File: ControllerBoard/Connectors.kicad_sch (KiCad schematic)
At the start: 2 parts, among them J1 X0511WVS-24AS-LPV01, J2 X0511WVS-24AS-LPV01

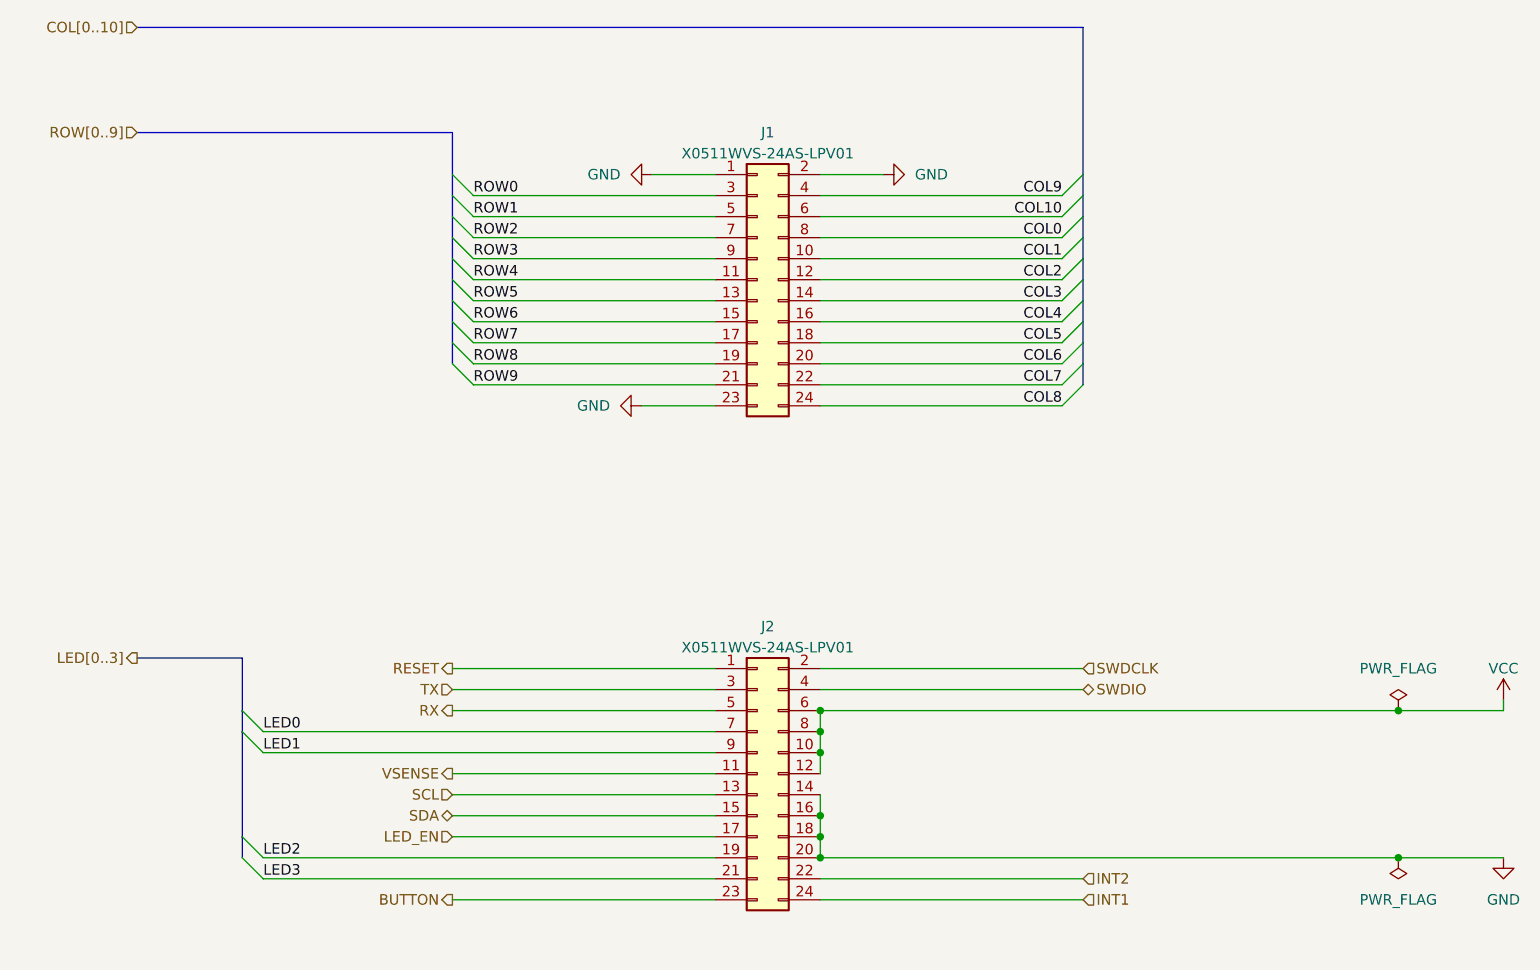
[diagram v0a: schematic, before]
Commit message: Remove LED driver
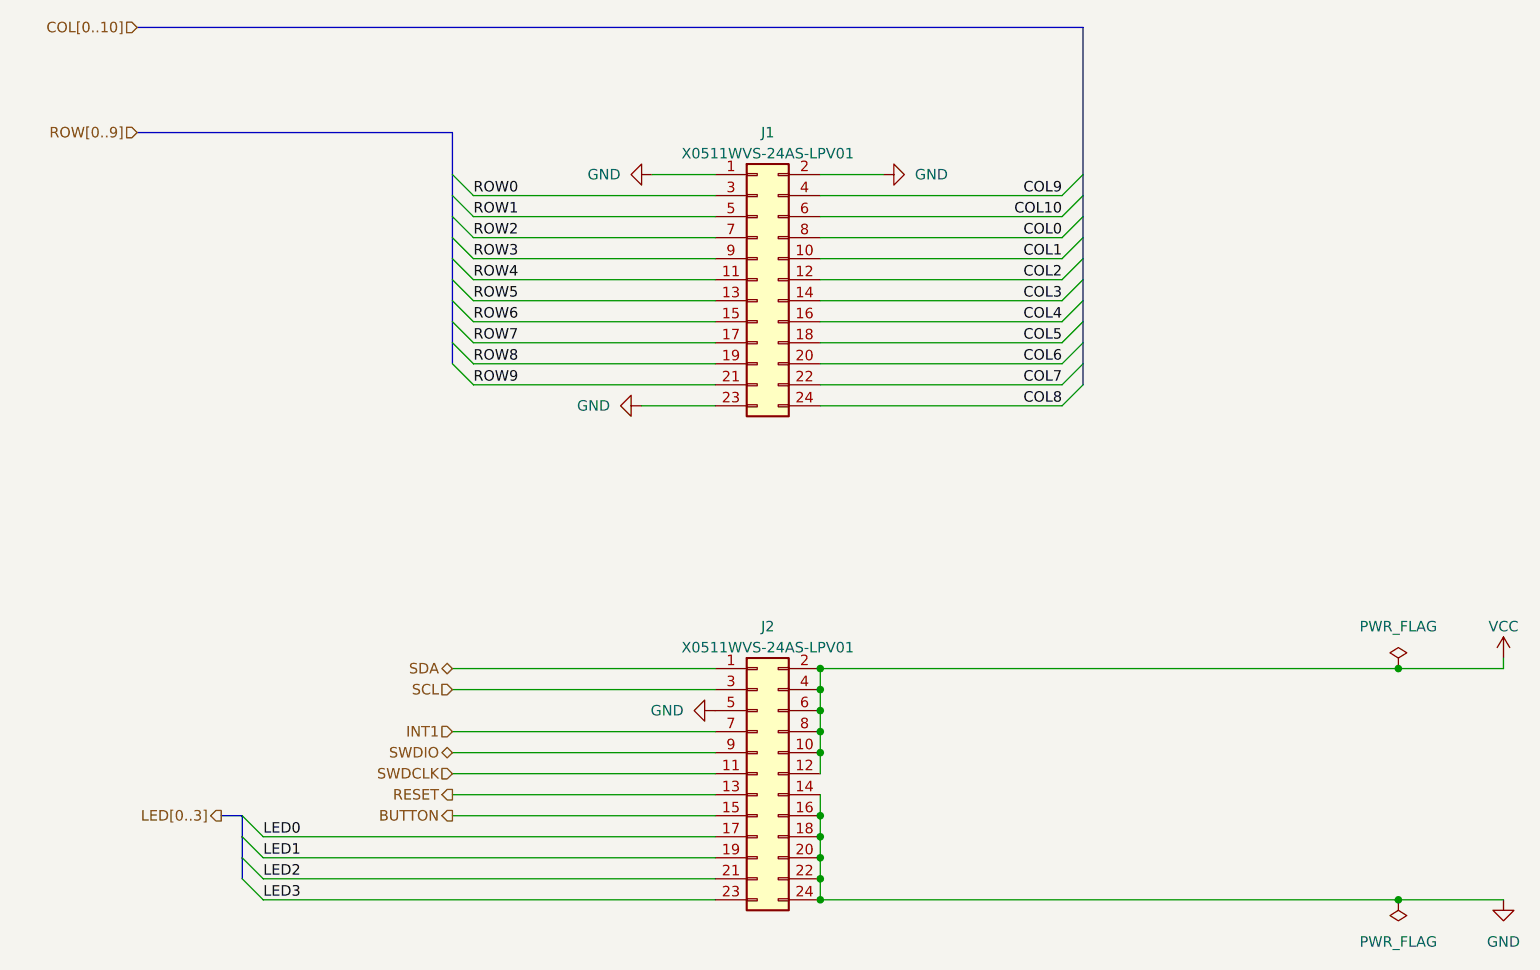
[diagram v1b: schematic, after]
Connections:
- net INT2 is gone; now on net GND: J2.22 (Pin_22)
- net LED_EN is gone; now on net LED0: J2.17 (Pin_17)
- net RX is gone; now on net GND: J2.5 (Pin_5)
- net TX is gone; now on net SCL: J2.3 (Pin_3)
- net VSENSE is gone; now on net SWDCLK: J2.11 (Pin_11)
- net BUTTON: now also J2.15 (Pin_15); no longer J2.23 (Pin_23)
- net GND: now also J2.24 (Pin_24)
- net INT1: now also J2.7 (Pin_7); no longer J2.24 (Pin_24)
- net LED0: no longer J2.7 (Pin_7)
- net LED1: now also J2.19 (Pin_19); no longer J2.9 (Pin_9)
- net LED2: now also J2.21 (Pin_21); no longer J2.19 (Pin_19)
- net LED3: now also J2.23 (Pin_23); no longer J2.21 (Pin_21)
- net RESET: now also J2.13 (Pin_13); no longer J2.1 (Pin_1)
- net SCL: no longer J2.13 (Pin_13)
- net SDA: now also J2.1 (Pin_1); no longer J2.15 (Pin_15)
- net SWDCLK: no longer J2.2 (Pin_2)
- net SWDIO: now also J2.9 (Pin_9); no longer J2.4 (Pin_4)
- net VCC: now also J2.2 (Pin_2), J2.4 (Pin_4)

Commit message: Change led matrix routing for sinking current through mcu, sourcing from battery
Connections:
- net BUTTON: now also J2.23 (Pin_23); no longer J2.15 (Pin_15)
- net COL0: now also J1.3 (Pin_3); no longer J1.8 (Pin_8)
- net COL1: now also J1.5 (Pin_5); no longer J1.10 (Pin_10)
- net COL10: now also J1.23 (Pin_23); no longer J1.6 (Pin_6)
- net COL2: now also J1.7 (Pin_7); no longer J1.12 (Pin_12)
- net COL3: now also J1.9 (Pin_9); no longer J1.14 (Pin_14)
- net COL4: now also J1.11 (Pin_11); no longer J1.16 (Pin_16)
- net COL5: now also J1.13 (Pin_13); no longer J1.18 (Pin_18)
- net COL6: now also J1.15 (Pin_15); no longer J1.20 (Pin_20)
- net COL7: now also J1.17 (Pin_17); no longer J1.22 (Pin_22)
- net COL8: now also J1.19 (Pin_19); no longer J1.24 (Pin_24)
- net COL9: now also J1.21 (Pin_21); no longer J1.4 (Pin_4)
- net GND: now also J1.24 (Pin_24); no longer J1.23 (Pin_23)
- net LED0: now also J2.15 (Pin_15); no longer J2.17 (Pin_17)
- net LED1: now also J2.17 (Pin_17); no longer J2.19 (Pin_19)
- net LED2: now also J2.19 (Pin_19); no longer J2.21 (Pin_21)
- net LED3: now also J2.21 (Pin_21); no longer J2.23 (Pin_23)
- net ROW0: now also J1.4 (Pin_4); no longer J1.3 (Pin_3)
- net ROW1: now also J1.6 (Pin_6); no longer J1.5 (Pin_5)
- net ROW2: now also J1.8 (Pin_8); no longer J1.7 (Pin_7)
- net ROW3: now also J1.10 (Pin_10); no longer J1.9 (Pin_9)
- net ROW4: now also J1.12 (Pin_12); no longer J1.11 (Pin_11)
- net ROW5: now also J1.14 (Pin_14); no longer J1.13 (Pin_13)
- net ROW6: now also J1.16 (Pin_16); no longer J1.15 (Pin_15)
- net ROW7: now also J1.18 (Pin_18); no longer J1.17 (Pin_17)
- net ROW8: now also J1.20 (Pin_20); no longer J1.19 (Pin_19)
- net ROW9: now also J1.22 (Pin_22); no longer J1.21 (Pin_21)
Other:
- title: (none) -> WordWatch - Controller Board
